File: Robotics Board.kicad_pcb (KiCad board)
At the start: 2 copper layers, 83 parts, among them CON1 DC_IN, J1 USB, P1 CONN_3, P10 CONN_6, P11 CONN_8, P12 CONN_20, P13 CONN_6, P14 CONN_20, P15 CONN_5, P16 CONN_20, P17 CONN_20, P18 CONN_20, P19 CONN_20, P2 CONN_3, P20 CONN_20, P21 CONN_20, P22 CONN_20, P23 CONN_1, P3 CONN_12, P4 CONN_12, P5 CONN_20, P6 CONN_20, P7 CONN_20, P8 CONN_8, P9 CONN_8, U1 7805, U2 L293, U3 PIC18F4550, X1 4MHz

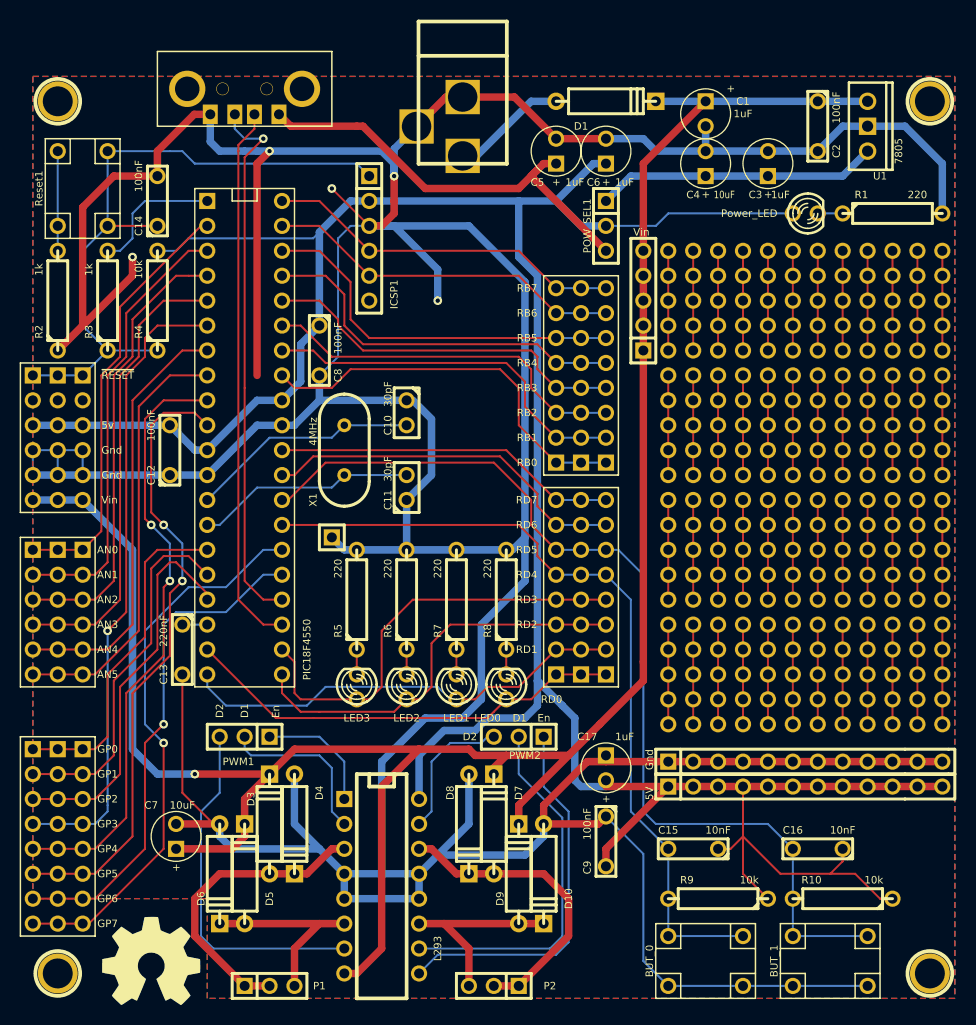
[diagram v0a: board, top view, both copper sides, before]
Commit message: Changed the footprint of the PIC to the correct one. Changed the layout of the development area, to be more suited for development Changed the layout of the reset button and programmer header. The programmer header now needs to be a 90deg header, for the pickit3 to fit Added components for the mounting holes and OSHW logos.
Signed-off-by: Kolijn Wolfaardt <kolijn.wolfaardt2gmail.com>
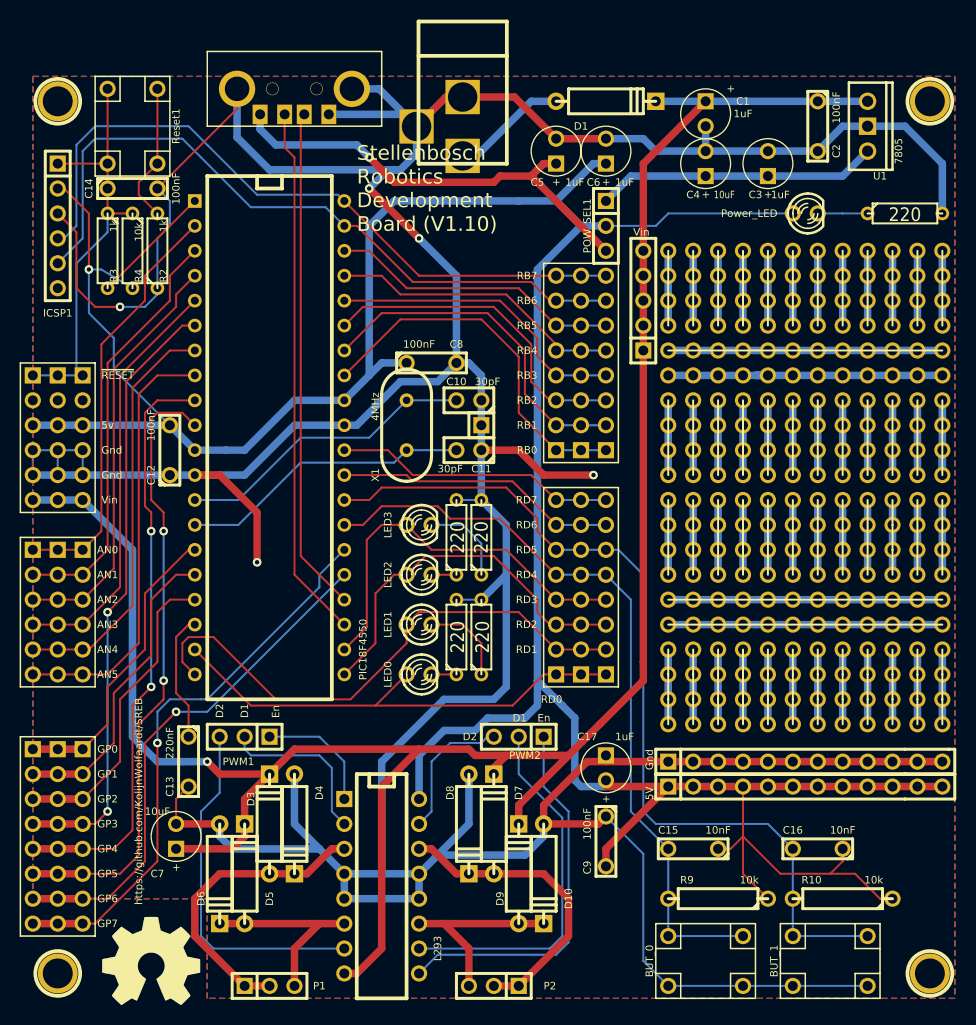
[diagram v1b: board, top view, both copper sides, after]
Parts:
- removed 1PIN (x4): P***, 1pin
- removed G***: OSHW-logo_copper-front_10mm, OSHW-logo_copper-front_10mm
- removed G***: OSHW-logo_silkscreen-front_10mm, OSHW-logo_silkscreen-front_10mm
- added MountingHole1: CONN_1, 1pin, F.Cu at (66.0, 54.6)
- added MountingHole2: CONN_1, 1pin, F.Cu at (154.9, 54.6)
- added MountingHole3: CONN_1, 1pin, F.Cu at (66.0, 143.5)
- added MountingHole4: CONN_1, 1pin, F.Cu at (154.9, 143.5)
- added OSHWLogoBack1: CONN_1, OSHW-logo_copper-back_10mm, B.Cu at (75.6, 142.2)
- added OSHWLogoFront1: CONN_1, OSHW-logo_silkscreen-front_10mm, F.Cu at (75.6, 142.2)
- R1, R2, R3, R4, R5, R6, R7, R8: footprint R4 -> R3
- U3: footprint DIP-40__300 -> DIP-40__600
- moved ICSP1 31.8 mm to (66.0, 67.3)
- moved P23 19.1 mm to (109.2, 87.6)
- moved LED3 17.7 mm to (102.9, 97.8), turned to 0 degrees
- moved R5 14.2 mm to (109.2, 99.1)
- moved C8 11.5 mm to (104.1, 81.3), turned to 0 degrees
- moved LED2 11.5 mm to (102.9, 102.9), turned to 0 degrees
- moved C13 11.4 mm to (79.4, 121.9)
- moved R2 11.4 mm to (76.2, 69.8)
- moved LED0 8.98 mm to (102.9, 113.0), turned to 0 degrees
- moved R6 8.13 mm to (106.7, 99.1)
- moved Reset1 8.13 mm to (73.7, 57.1), turned to 270 degrees
- moved C11 7.41 mm to (108.0, 90.2), turned to 180 degrees
- moved LED1 7.41 mm to (102.9, 108.0), turned to 0 degrees
- moved X1 6.84 mm to (101.6, 87.6)
- moved C10 6.48 mm to (108.0, 85.1), turned to 180 degrees
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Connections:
- J1 pad 5: (no net) -> Gnd
- J1 pad 6: (no net) -> Gnd
- P12 pad 1: N-0000037 -> N-0000059
- P12 pad 10: N-0000038 -> N-0000057
- P12 pad 11: N-0000039 -> N-0000058
- P12 pad 12: N-0000039 -> N-0000058
- P12 pad 13: N-0000039 -> N-0000058
- P12 pad 14: N-0000039 -> N-0000058
- P12 pad 15: N-0000039 -> N-0000061
- P12 pad 16: N-0000052 -> N-0000068
- P12 pad 17: N-0000052 -> N-0000062
- P12 pad 18: N-0000052 -> N-0000062
- P12 pad 19: N-0000052 -> N-0000062
- P12 pad 2: N-0000037 -> N-0000059
- P12 pad 20: N-0000052 -> N-0000062
- P12 pad 3: N-0000037 -> N-0000059
- P12 pad 4: N-0000037 -> N-0000059
- P12 pad 5: N-0000037 -> N-0000064
- P12 pad 6: N-0000038 -> N-0000078
- P12 pad 7: N-0000038 -> N-0000057
- P12 pad 8: N-0000038 -> N-0000057
- P12 pad 9: N-0000038 -> N-0000057
- P14 pad 1: N-0000057 -> N-0000063
- P14 pad 10: N-0000058 -> N-0000065
- P14 pad 11: N-0000047 -> N-0000055
- P14 pad 12: N-0000047 -> N-0000055
- P14 pad 13: N-0000047 -> N-0000055
- P14 pad 14: N-0000047 -> N-0000055
- P14 pad 15: N-0000047 -> N-0000061
- P14 pad 16: N-0000048 -> N-0000068
- P14 pad 17: N-0000048 -> N-0000054
- P14 pad 18: N-0000048 -> N-0000054
- P14 pad 19: N-0000048 -> N-0000054
- P14 pad 2: N-0000057 -> N-0000063
- P14 pad 20: N-0000048 -> N-0000054
- P14 pad 3: N-0000057 -> N-0000063
- P14 pad 4: N-0000057 -> N-0000063
- P14 pad 5: N-0000057 -> N-0000064
- P14 pad 6: N-0000058 -> N-0000078
- P14 pad 7: N-0000058 -> N-0000065
- P14 pad 8: N-0000058 -> N-0000065
- P14 pad 9: N-0000058 -> N-0000065
- P16 pad 1: N-0000069 -> N-0000074
- P16 pad 10: N-0000070 -> N-0000080
- P16 pad 11: N-0000071 -> N-0000049
- P16 pad 12: N-0000071 -> N-0000049
- P16 pad 13: N-0000071 -> N-0000049
- P16 pad 14: N-0000071 -> N-0000049
- P16 pad 15: N-0000071 -> N-0000061
- P16 pad 16: N-0000072 -> N-0000068
- P16 pad 17: N-0000072 -> N-0000048
- P16 pad 18: N-0000072 -> N-0000048
- P16 pad 19: N-0000072 -> N-0000048
- P16 pad 2: N-0000069 -> N-0000074
- P16 pad 20: N-0000072 -> N-0000048
- P16 pad 3: N-0000069 -> N-0000074
- P16 pad 4: N-0000069 -> N-0000074
- P16 pad 5: N-0000069 -> N-0000064
- P16 pad 6: N-0000070 -> N-0000078
- P16 pad 7: N-0000070 -> N-0000080
- P16 pad 8: N-0000070 -> N-0000080
- P16 pad 9: N-0000070 -> N-0000080
- P17 pad 1: N-0000065 -> N-0000082
- P17 pad 10: N-0000075 -> N-0000083
- P17 pad 11: N-0000076 -> N-0000084
- P17 pad 12: N-0000076 -> N-0000084
- P17 pad 13: N-0000076 -> N-0000084
- P17 pad 14: N-0000076 -> N-0000084
- P17 pad 15: N-0000076 -> N-0000061
- P17 pad 16: N-0000077 -> N-0000068
- P17 pad 17: N-0000077 -> N-0000073
- P17 pad 18: N-0000077 -> N-0000073
- P17 pad 19: N-0000077 -> N-0000073
- P17 pad 2: N-0000065 -> N-0000082
- P17 pad 20: N-0000077 -> N-0000073
- P17 pad 3: N-0000065 -> N-0000082
- P17 pad 4: N-0000065 -> N-0000082
- P17 pad 5: N-0000065 -> N-0000064
- P17 pad 6: N-0000075 -> N-0000078
- P17 pad 7: N-0000075 -> N-0000083
- P17 pad 8: N-0000075 -> N-0000083
- P17 pad 9: N-0000075 -> N-0000083
- P18 pad 1: N-0000078 -> N-0000071
- P18 pad 10: N-0000079 -> N-0000072
- P18 pad 11: N-0000080 -> N-0000076
- P18 pad 12: N-0000080 -> N-0000076
- P18 pad 13: N-0000080 -> N-0000076
- P18 pad 14: N-0000080 -> N-0000076
- P18 pad 15: N-0000080 -> N-0000061
- P18 pad 16: N-0000081 -> N-0000068
- P18 pad 17: N-0000081 -> N-0000075
- P18 pad 18: N-0000081 -> N-0000075
- P18 pad 19: N-0000081 -> N-0000075
- P18 pad 2: N-0000078 -> N-0000071
- P18 pad 20: N-0000081 -> N-0000075
- P18 pad 3: N-0000078 -> N-0000071
- P18 pad 4: N-0000078 -> N-0000071
- P18 pad 5: N-0000078 -> N-0000064
- P18 pad 6: N-0000079 -> N-0000078
- P18 pad 7: N-0000079 -> N-0000072
- P18 pad 8: N-0000079 -> N-0000072
- P18 pad 9: N-0000079 -> N-0000072
- P19 pad 1: N-0000046 -> N-0000045
- P19 pad 10: N-0000036 -> N-0000044
- P19 pad 11: N-0000034 -> N-0000043
- P19 pad 12: N-0000034 -> N-0000043
- P19 pad 13: N-0000034 -> N-0000043
- P19 pad 14: N-0000034 -> N-0000043
- P19 pad 15: N-0000034 -> N-0000061
- P19 pad 16: N-0000035 -> N-0000068
- P19 pad 17: N-0000035 -> N-0000060
- P19 pad 18: N-0000035 -> N-0000060
- P19 pad 19: N-0000035 -> N-0000060
- P19 pad 2: N-0000046 -> N-0000045
- P19 pad 20: N-0000035 -> N-0000060
- P19 pad 3: N-0000046 -> N-0000045
- P19 pad 4: N-0000046 -> N-0000045
- P19 pad 5: N-0000046 -> N-0000064
- P19 pad 6: N-0000036 -> N-0000078
- P19 pad 7: N-0000036 -> N-0000044
- P19 pad 8: N-0000036 -> N-0000044
- P19 pad 9: N-0000036 -> N-0000044
- P20 pad 1: N-0000053 -> N-0000090
- P20 pad 10: N-0000054 -> N-0000087
- P20 pad 11: N-0000055 -> N-0000086
- P20 pad 12: N-0000055 -> N-0000086
- P20 pad 13: N-0000055 -> N-0000086
- P20 pad 14: N-0000055 -> N-0000086
- P20 pad 15: N-0000055 -> N-0000061
- P20 pad 16: N-0000056 -> N-0000068
- P20 pad 17: N-0000056 -> N-0000085
- P20 pad 18: N-0000056 -> N-0000085
- P20 pad 19: N-0000056 -> N-0000085
- P20 pad 2: N-0000053 -> N-0000090
- P20 pad 20: N-0000056 -> N-0000085
- P20 pad 3: N-0000053 -> N-0000090
- P20 pad 4: N-0000053 -> N-0000090
- P20 pad 5: N-0000053 -> N-0000064
- P20 pad 6: N-0000054 -> N-0000078
- P20 pad 7: N-0000054 -> N-0000087
- P20 pad 8: N-0000054 -> N-0000087
- P20 pad 9: N-0000054 -> N-0000087
- P21 pad 1: N-0000049 -> N-0000089
- P21 pad 10: N-0000050 -> N-0000088
- P21 pad 11: N-0000051 -> N-0000092
- P21 pad 12: N-0000051 -> N-0000092
- P21 pad 13: N-0000051 -> N-0000092
- P21 pad 14: N-0000051 -> N-0000092
- P21 pad 15: N-0000051 -> N-0000061
- P21 pad 16: N-0000062 -> N-0000068
- P21 pad 17: N-0000062 -> N-0000091
- P21 pad 18: N-0000062 -> N-0000091
- P21 pad 19: N-0000062 -> N-0000091
- P21 pad 2: N-0000049 -> N-0000089
- P21 pad 20: N-0000062 -> N-0000091
- P21 pad 3: N-0000049 -> N-0000089
- P21 pad 4: N-0000049 -> N-0000089
- P21 pad 5: N-0000049 -> N-0000064
- P21 pad 6: N-0000050 -> N-0000078
- P21 pad 7: N-0000050 -> N-0000088
- P21 pad 8: N-0000050 -> N-0000088
- P21 pad 9: N-0000050 -> N-0000088
- P22 pad 1: N-0000073 -> N-0000047
- P22 pad 10: N-0000074 -> N-0000053
- P22 pad 11: N-0000040 -> N-0000050
- P22 pad 12: N-0000040 -> N-0000050
- P22 pad 13: N-0000040 -> N-0000050
- P22 pad 14: N-0000040 -> N-0000050
- P22 pad 15: N-0000040 -> N-0000061
- P22 pad 16: N-0000041 -> N-0000068
- P22 pad 17: N-0000041 -> N-0000051
- P22 pad 18: N-0000041 -> N-0000051
- P22 pad 19: N-0000041 -> N-0000051
- P22 pad 2: N-0000073 -> N-0000047
- P22 pad 20: N-0000041 -> N-0000051
- P22 pad 3: N-0000073 -> N-0000047
- P22 pad 4: N-0000073 -> N-0000047
- P22 pad 5: N-0000073 -> N-0000064
- P22 pad 6: N-0000074 -> N-0000078
- P22 pad 7: N-0000074 -> N-0000053
- P22 pad 8: N-0000074 -> N-0000053
- P22 pad 9: N-0000074 -> N-0000053
- P5 pad 10: N-0000067 -> N-0000070
- P5 pad 11: N-0000068 -> N-0000069
- P5 pad 12: N-0000068 -> N-0000069
- P5 pad 13: N-0000068 -> N-0000069
- P5 pad 14: N-0000068 -> N-0000069
- P5 pad 15: N-0000068 -> N-0000061
- P5 pad 16: N-0000059 -> N-0000068
- P5 pad 17: N-0000059 -> N-0000067
- P5 pad 18: N-0000059 -> N-0000067
- P5 pad 19: N-0000059 -> N-0000067
- P5 pad 20: N-0000059 -> N-0000067
- P5 pad 5: N-0000066 -> N-0000064
- P5 pad 6: N-0000067 -> N-0000078
- P5 pad 7: N-0000067 -> N-0000070
- P5 pad 8: N-0000067 -> N-0000070
- P5 pad 9: N-0000067 -> N-0000070
- P6 pad 1: N-0000060 -> N-0000079
- P6 pad 10: N-0000061 -> N-0000077
- P6 pad 11: N-0000063 -> N-0000056
- P6 pad 12: N-0000063 -> N-0000056
- P6 pad 13: N-0000063 -> N-0000056
- P6 pad 14: N-0000063 -> N-0000056
- P6 pad 15: N-0000063 -> N-0000061
- P6 pad 16: N-0000064 -> N-0000068
- P6 pad 17: N-0000064 -> N-0000081
- P6 pad 18: N-0000064 -> N-0000081
- P6 pad 19: N-0000064 -> N-0000081
- P6 pad 2: N-0000060 -> N-0000079
- P6 pad 20: N-0000064 -> N-0000081
- P6 pad 3: N-0000060 -> N-0000079
- P6 pad 4: N-0000060 -> N-0000079
- P6 pad 5: N-0000060 -> N-0000064
- P6 pad 6: N-0000061 -> N-0000078
- P6 pad 7: N-0000061 -> N-0000077
- P6 pad 8: N-0000061 -> N-0000077
- P6 pad 9: N-0000061 -> N-0000077
- P7 pad 1: N-0000042 -> N-0000052
- P7 pad 10: N-0000043 -> N-0000042
- P7 pad 11: N-0000044 -> N-0000041
- P7 pad 12: N-0000044 -> N-0000041
- P7 pad 13: N-0000044 -> N-0000041
- P7 pad 14: N-0000044 -> N-0000041
- P7 pad 15: N-0000044 -> N-0000061
- P7 pad 16: N-0000045 -> N-0000068
- P7 pad 17: N-0000045 -> N-0000046
- P7 pad 18: N-0000045 -> N-0000046
- P7 pad 19: N-0000045 -> N-0000046
- P7 pad 2: N-0000042 -> N-0000052
- P7 pad 20: N-0000045 -> N-0000046
- P7 pad 3: N-0000042 -> N-0000052
- P7 pad 4: N-0000042 -> N-0000052
- P7 pad 5: N-0000042 -> N-0000064
- P7 pad 6: N-0000043 -> N-0000078
- P7 pad 7: N-0000043 -> N-0000042
- P7 pad 8: N-0000043 -> N-0000042
- P7 pad 9: N-0000043 -> N-0000042
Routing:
- net Gnd: track 638.7 -> 534.9 mm
- net /Microcontroller/RB6: track 36.7 -> 73.2 mm
- net /Microcontroller/RB7: track 36.7 -> 71.8 mm
- net /Microcontroller/~RESET: track 69.0 -> 43.5 mm
- net N-0000061: track 10.2 -> 30.5 mm
- net N-0000078: track 10.2 -> 27.9 mm
- net N-0000068: track 10.2 -> 27.9 mm
- net N-0000064: track 10.2 -> 27.9 mm
- net V_5v: track 367.1 -> 350.2 mm, vias 0 -> 1
- net /Microcontroller/Vusb: track 2.54 -> 13.1 mm
- net N-0000035: track 10.2 -> 0.00 mm
- net N-0000040: track 10.2 -> 0.00 mm
- net N-0000039: track 10.2 -> 0.00 mm
- net N-0000038: track 10.2 -> 0.00 mm
- net N-0000037: track 10.2 -> 0.00 mm
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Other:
- board text added: "Stellenbosch Robotics Development Board (V1.10)"
- board text added: "https://github.com/KolijnWolfaardt/SREB"

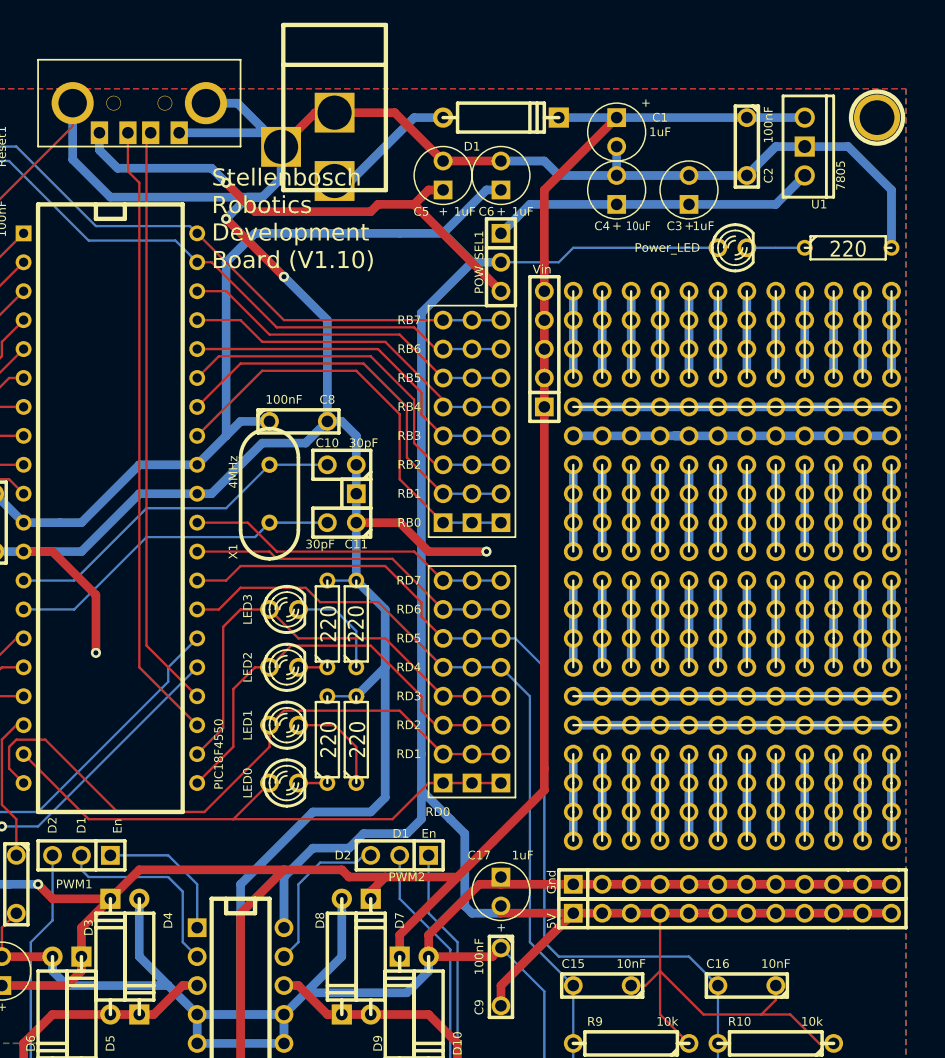
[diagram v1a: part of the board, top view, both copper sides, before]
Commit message: Changed to FTDI chip, cut space from development area
An FTDI chip was added to provide the USB communications rather than the PIC
A jumper is available to choose if the USB datalines go to the FTDI chip or the
PIC.

The development area was reduced to provide space for the FTDI chip.

Signed-off-by: Kolijn Wolfaardt <kolijn.wolfaardt@gmail.com>
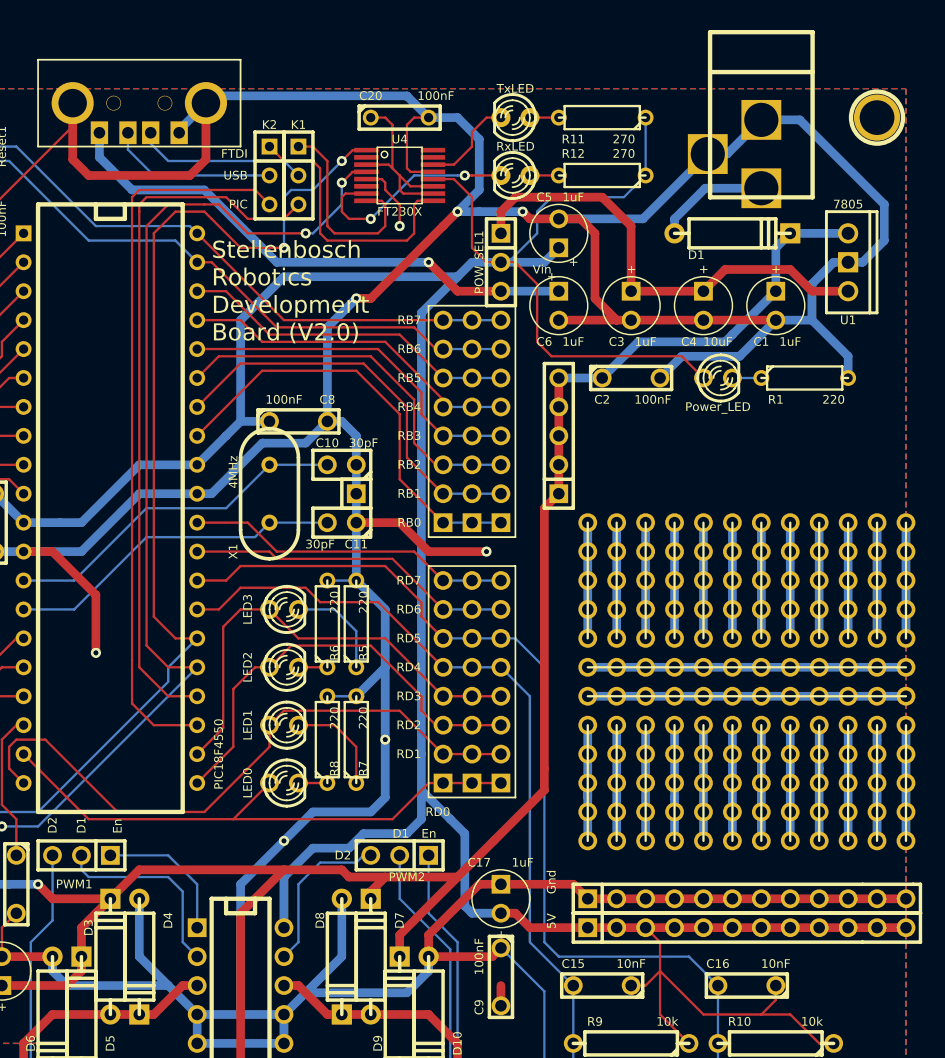
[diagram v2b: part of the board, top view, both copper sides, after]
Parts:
- added C20: 100nF, C2, F.Cu at (113.0, 54.6)
- added D11: TxLED, LED-3MM, F.Cu at (123.2, 54.6)
- added D12: RxLED, LED-3MM, F.Cu at (123.2, 59.7)
- added K1: CONN_3, SIL-3, F.Cu at (104.1, 59.7)
- added K2: CONN_3, SIL-3, F.Cu at (101.6, 59.7)
- added R11: 270, R3, F.Cu at (130.8, 54.6)
- added R12: 270, R3, F.Cu at (130.8, 59.7)
- added U4: FT230X, ssop-16-extended, F.Cu at (113.0, 59.7)
- P12, P14, P16, P17, P18, P19, P20, P21, P22, P5, P6, P7: value CONN_20 -> CONN_12; footprint SIL-20-No-Silk -> SIL-12-No-Silk
- moved CON1 37.5 mm to (144.8, 54.6)
- moved D1 22.7 mm to (142.2, 64.8)
- moved C2 22.7 mm to (133.3, 77.5), turned to 0 degrees
- moved C1 20.7 mm to (146.1, 71.1)
- moved C5 15.3 mm to (127.0, 71.1), turned to 270 degrees
- moved C4 12.7 mm to (139.7, 71.1), turned to 270 degrees
- moved R1 12.0 mm to (148.6, 77.5)
- moved D2 11.5 mm to (141.0, 77.5)
- moved C3 11.4 mm to (133.3, 71.1), turned to 270 degrees
- moved U1 10.9 mm to (152.4, 67.3)
- moved P15 7.73 mm to (127.0, 81.3)
- moved C6 7.18 mm to (127.0, 64.8)
- moved P4 1.80 mm to (143.5, 125.7)
- moved P3 1.80 mm to (143.5, 123.2)
- moved P12 1.27 mm to (137.2, 95.2)
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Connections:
- J1 pad 2: /Microcontroller/USB_D- -> N-0000082
- J1 pad 3: /Microcontroller/USB_D+ -> N-0000089
- P12 pad 1: N-0000059 -> N-0000061
- P12 pad 10: N-0000057 -> N-0000048
- P12 pad 11: N-0000058 -> N-0000048
- P12 pad 12: N-0000058 -> N-0000048
- P12 pad 2: N-0000059 -> N-0000061
- P12 pad 3: N-0000059 -> N-0000061
- P12 pad 4: N-0000059 -> N-0000061
- P12 pad 5: N-0000064 -> N-0000061
- P12 pad 7: N-0000057 -> N-0000047
- P12 pad 8: N-0000057 -> N-0000048
- P12 pad 9: N-0000057 -> N-0000048
- P14 pad 1: N-0000063 -> N-0000046
- P14 pad 10: N-0000065 -> N-0000049
- P14 pad 11: N-0000055 -> N-0000049
- P14 pad 12: N-0000055 -> N-0000049
- P14 pad 2: N-0000063 -> N-0000046
- P14 pad 3: N-0000063 -> N-0000046
- P14 pad 4: N-0000063 -> N-0000046
- P14 pad 5: N-0000064 -> N-0000046
- P14 pad 7: N-0000065 -> N-0000047
- P14 pad 8: N-0000065 -> N-0000049
- P14 pad 9: N-0000065 -> N-0000049
- P16 pad 1: N-0000074 (its old number) -> N-0000042
- P16 pad 10: N-0000080 (its old number) -> N-0000041
- P16 pad 11: N-0000049 -> N-0000041
- P16 pad 12: N-0000049 -> N-0000041
- P16 pad 2: N-0000074 (its old number) -> N-0000042
- P16 pad 3: N-0000074 (its old number) -> N-0000042
- P16 pad 4: N-0000074 (its old number) -> N-0000042
- P16 pad 5: N-0000064 -> N-0000042
- P16 pad 7: N-0000080 (its old number) -> N-0000047
- P16 pad 8: N-0000080 (its old number) -> N-0000041
- P16 pad 9: N-0000080 (its old number) -> N-0000041
- P17 pad 1: N-0000082 -> N-0000043
- P17 pad 10: N-0000083 -> N-0000044
- P17 pad 11: N-0000084 -> N-0000044
- P17 pad 12: N-0000084 -> N-0000044
- P17 pad 2: N-0000082 -> N-0000043
- P17 pad 3: N-0000082 -> N-0000043
- P17 pad 4: N-0000082 -> N-0000043
- P17 pad 5: N-0000064 -> N-0000043
- P17 pad 7: N-0000083 -> N-0000047
- P17 pad 8: N-0000083 -> N-0000044
- P17 pad 9: N-0000083 -> N-0000044
- P18 pad 1: N-0000071 (its old number) -> N-0000054
- P18 pad 10: N-0000072 (its old number) -> N-0000055
- P18 pad 11: N-0000076 (its old number) -> N-0000055
- P18 pad 12: N-0000076 (its old number) -> N-0000055
- P18 pad 2: N-0000071 (its old number) -> N-0000054
- P18 pad 3: N-0000071 (its old number) -> N-0000054
- P18 pad 4: N-0000071 (its old number) -> N-0000054
- P18 pad 5: N-0000064 -> N-0000054
- P18 pad 7: N-0000072 (its old number) -> N-0000047
- P18 pad 8: N-0000072 (its old number) -> N-0000055
- P18 pad 9: N-0000072 (its old number) -> N-0000055
- P19 pad 1: N-0000045 (its old number) -> N-0000056
- P19 pad 10: N-0000044 -> N-0000050
- P19 pad 11: N-0000043 -> N-0000050
- P19 pad 12: N-0000043 -> N-0000050
- P19 pad 2: N-0000045 (its old number) -> N-0000056
- P19 pad 3: N-0000045 (its old number) -> N-0000056
- P19 pad 4: N-0000045 (its old number) -> N-0000056
- P19 pad 5: N-0000064 -> N-0000056
- P19 pad 7: N-0000044 -> N-0000047
- P19 pad 8: N-0000044 -> N-0000050
- P19 pad 9: N-0000044 -> N-0000050
- P20 pad 1: N-0000090 -> N-0000051
- P20 pad 10: N-0000087 (its old number) -> N-0000052
- P20 pad 11: N-0000086 -> N-0000052
- P20 pad 12: N-0000086 -> N-0000052
- P20 pad 2: N-0000090 -> N-0000051
- P20 pad 3: N-0000090 -> N-0000051
- P20 pad 4: N-0000090 -> N-0000051
- P20 pad 5: N-0000064 -> N-0000051
- P20 pad 7: N-0000087 (its old number) -> N-0000047
- P20 pad 8: N-0000087 (its old number) -> N-0000052
- P20 pad 9: N-0000087 (its old number) -> N-0000052
- P21 pad 1: N-0000089 -> N-0000053
- P21 pad 10: N-0000088 -> N-0000065
- P21 pad 11: N-0000092 -> N-0000065
- P21 pad 12: N-0000092 -> N-0000065
- P21 pad 2: N-0000089 -> N-0000053
- P21 pad 3: N-0000089 -> N-0000053
- P21 pad 4: N-0000089 -> N-0000053
- P21 pad 5: N-0000064 -> N-0000053
- P21 pad 7: N-0000088 -> N-0000047
- P21 pad 8: N-0000088 -> N-0000065
- P21 pad 9: N-0000088 -> N-0000065
- P22 pad 1: N-0000047 -> N-0000066
- P22 pad 10: N-0000053 -> N-0000067
- P22 pad 11: N-0000050 -> N-0000067
- P22 pad 12: N-0000050 -> N-0000067
- P22 pad 2: N-0000047 -> N-0000066
- P22 pad 3: N-0000047 -> N-0000066
- P22 pad 4: N-0000047 -> N-0000066
- P22 pad 5: N-0000064 -> N-0000066
- P22 pad 7: N-0000053 -> N-0000047
- P22 pad 8: N-0000053 -> N-0000067
- P22 pad 9: N-0000053 -> N-0000067
- P5 pad 1: N-0000066 -> N-0000062
- P5 pad 10: N-0000070 (its old number) -> N-0000063
- P5 pad 11: N-0000069 (its old number) -> N-0000063
- P5 pad 12: N-0000069 (its old number) -> N-0000063
- P5 pad 2: N-0000066 -> N-0000062
- P5 pad 3: N-0000066 -> N-0000062
- P5 pad 4: N-0000066 -> N-0000062
- P5 pad 5: N-0000064 -> N-0000062
- P5 pad 7: N-0000070 (its old number) -> N-0000047
- P5 pad 8: N-0000070 (its old number) -> N-0000063
- P5 pad 9: N-0000070 (its old number) -> N-0000063
- P6 pad 1: N-0000079 (its old number) -> N-0000064
- P6 pad 10: N-0000077 (its old number) -> N-0000058
- P6 pad 11: N-0000056 -> N-0000058
- P6 pad 12: N-0000056 -> N-0000058
- P6 pad 2: N-0000079 (its old number) -> N-0000064
- P6 pad 3: N-0000079 (its old number) -> N-0000064
- P6 pad 4: N-0000079 (its old number) -> N-0000064
- P6 pad 7: N-0000077 (its old number) -> N-0000047
- P6 pad 8: N-0000077 (its old number) -> N-0000058
- P6 pad 9: N-0000077 (its old number) -> N-0000058
- P7 pad 1: N-0000052 -> N-0000059
- P7 pad 10: N-0000042 -> N-0000060
- P7 pad 11: N-0000041 -> N-0000060
- P7 pad 12: N-0000041 -> N-0000060
- P7 pad 2: N-0000052 -> N-0000059
- P7 pad 3: N-0000052 -> N-0000059
- P7 pad 4: N-0000052 -> N-0000059
- P7 pad 5: N-0000064 -> N-0000059
- P7 pad 7: N-0000042 -> N-0000047
- P7 pad 8: N-0000042 -> N-0000060
- P7 pad 9: N-0000042 -> N-0000060
- U3 pad 23: /Microcontroller/USB_D- -> /Microcontroller/PIC_USB_D-
- U3 pad 24: /Microcontroller/USB_D+ -> /Microcontroller/PIC_USB_D+
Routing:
- net /Microcontroller/GP6: track 52.5 -> 119.1 mm, vias 1 -> 3
- net /Microcontroller/GP7: track 57.2 -> 122.4 mm, vias 1 -> 3
- net /Microcontroller/PIC_USB_D-: track 0.00 -> 63.8 mm
- net /Microcontroller/PIC_USB_D+: track 0.00 -> 62.3 mm
- net Gnd: track 534.9 -> 595.5 mm, vias 5 -> 9
- net /Microcontroller/USB_D+: track 51.5 -> 18.1 mm
- net /Microcontroller/USB_D-: track 54.5 -> 24.1 mm
- net N-0000068 (its old number): track 27.9 -> 0.00 mm
- net N-0000061: track 30.5 -> 10.2 mm
- net N-0000047: track 7.62 -> 27.9 mm
- net /Microcontroller/CBUS2: track 0.00 -> 19.4 mm, vias 0 -> 2
- net N-0000064: track 27.9 -> 10.2 mm
- net /Microcontroller/VCCIO: track 0.00 -> 16.9 mm
- net V_batt: track 225.9 -> 212.2 mm
- net N-0000069: track 28.8 -> 41.9 mm
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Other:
- board text added: "FTDI"
- board text added: "PIC"
- board text added: "Stellenbosch Robotics Development Board (V2.0)"
- board text added: "USB"
- board text removed: "Stellenbosch Robotics Development Board (V1.10)"
